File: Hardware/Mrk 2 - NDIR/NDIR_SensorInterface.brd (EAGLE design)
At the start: 26 x 49.7 mm, 6 parts, among them J1 CONN_I2C_SENSOR_BOARD_MOUNT_T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, J2 CONN_42.54, Q1 DMG3404

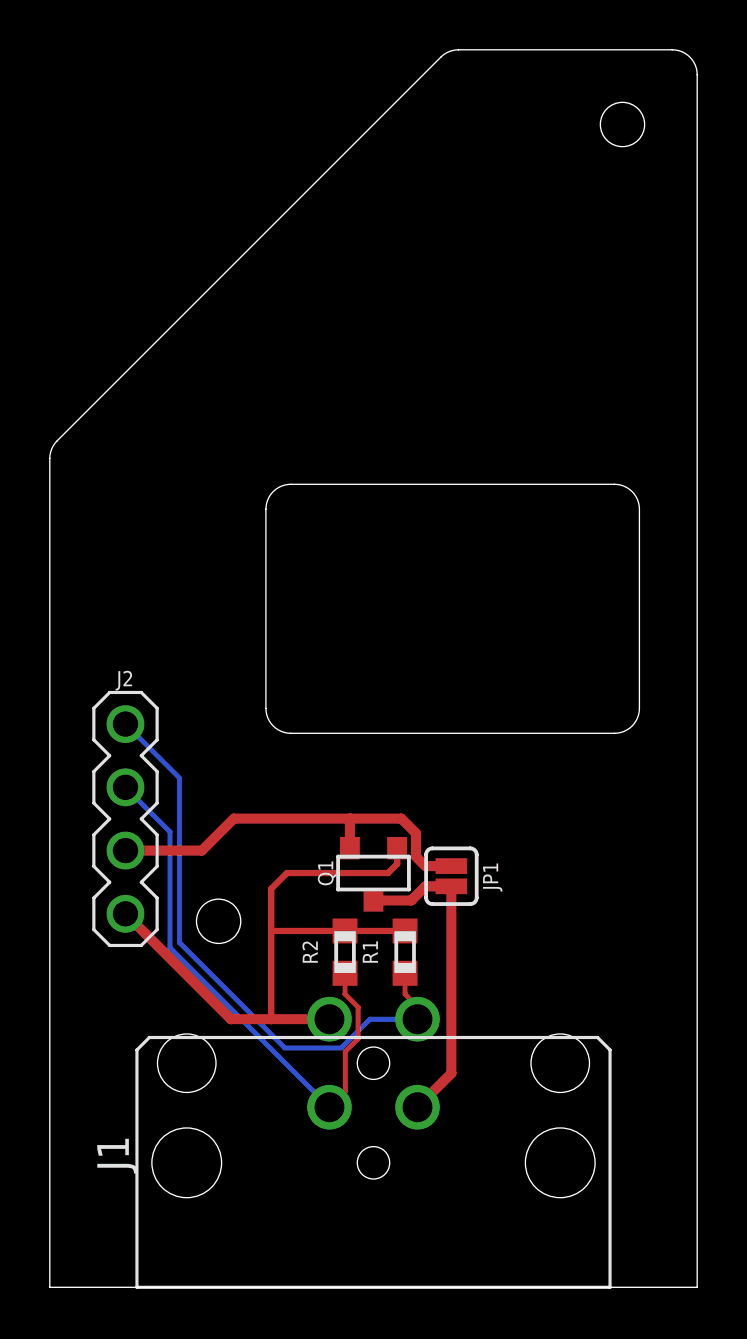
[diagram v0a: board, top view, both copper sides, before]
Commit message: Fixed production version naming of Mrk 2 design
Added layout dimensions
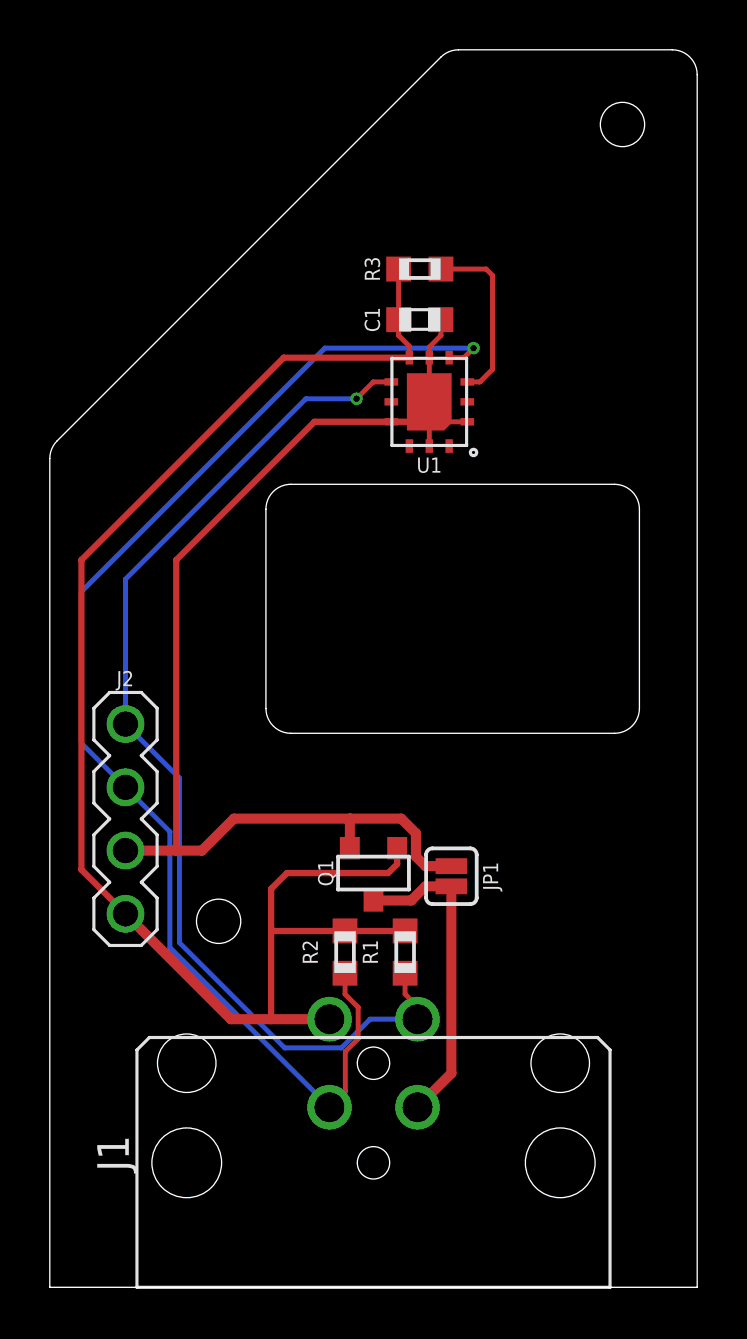
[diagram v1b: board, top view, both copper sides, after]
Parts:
- added C1: 0.1uF, bschulz_passives:C0603
- added R3: DNP, bschulz_passives:R0603
- added U1: STC31, bschulz:STC31
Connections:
- new net N$2: R3.1, U1.3
- net GND: now also C1.2, U1.1, U1.11, U1.5, U1.9, U1.EP
- net SCL: now also U1.4
- net SDA: now also U1.7
- net VIN+: now also C1.1, R3.2, U1.6
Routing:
- net VIN+: track 26.7 -> 61.9 mm
- net GND: track 16.2 -> 47.7 mm
- net SCL: track 22.3 -> 51.8 mm, vias 0 -> 1
- net SDA: track 23.5 -> 43.3 mm, vias 0 -> 1
- net N$2: track 0.00 -> 7.17 mm
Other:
- board text added: "Project Hedorah NDIR - SCD30 v1.1"
- board text removed: "Project Hedorah NDIR - SCD30 v1.0"
